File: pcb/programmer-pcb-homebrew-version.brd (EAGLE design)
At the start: 17 x 56.9 mm, 10 parts, among them IC1 MEGA8-AI, IC2 FT232RL, Q1 16 MHz

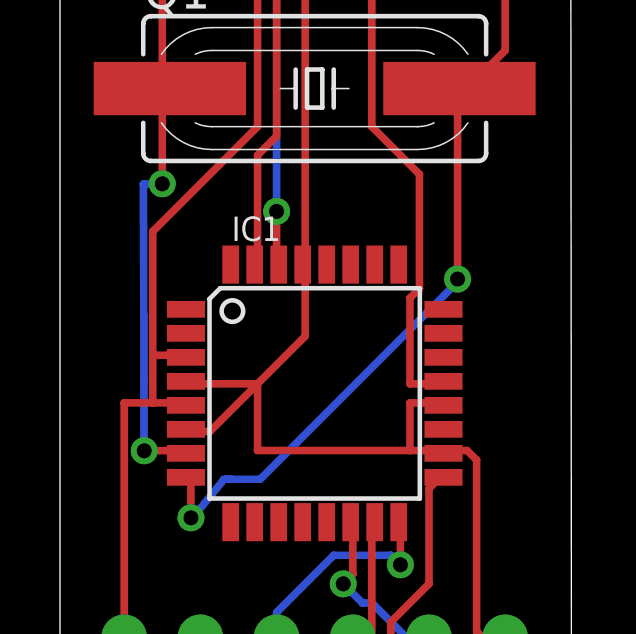
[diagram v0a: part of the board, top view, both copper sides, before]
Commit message: Revert "Minor changes"
This reverts commit 5d468dcfe678118c8d189d65b8291410209d50cf.
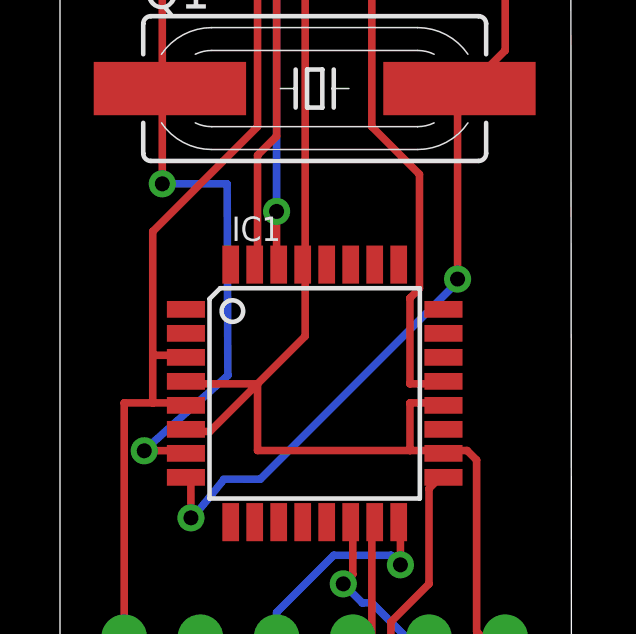
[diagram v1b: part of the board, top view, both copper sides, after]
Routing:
- net N$4: track 10.7 -> 12.2 mm
- net S$28: track 8.90 -> 10.2 mm
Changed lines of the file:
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@@
 <contactref element="C2" pad="1"/>
 <contactref element="Q1" pad="1"/>
-<wire x1="5.08" y1="19.685" x2="4.44785625" y2="19.67254375" width="0.254" layer="16"/>
+<wire x1="5.08" y1="19.685" x2="7.240178125" y2="19.685" width="0.254" layer="16"/>
 <wire x1="5.08" y1="22.86" x2="5.08" y2="19.685" width="0.254" layer="1"/>
 <wire x1="5.08" y1="22.86" x2="5.08" y2="29.21" width="0.254" layer="1"/>
@@
 </signal>
 <signal name="S$28">
-<wire x1="4.44874375" y1="19.67405" x2="4.47365" y2="13.184984375" width="0.254" layer="16"/>
-<wire x1="4.47365" y1="13.184984375" x2="4.468321875" y2="10.791303125" width="0.254" layer="16"/>
+<wire x1="7.241165625" y1="19.67993125" x2="7.265975" y2="13.297084375" width="0.254" layer="16"/>
+<wire x1="7.265975" y1="13.297084375" x2="4.468321875" y2="10.791303125" width="0.254" layer="16"/>
 <wire x1="4.468321875" y1="10.791303125" x2="4.47433125" y2="10.780275" width="0.254" layer="16"/>
 </signal>

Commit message: Minor changes
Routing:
- net N$4: track 12.2 -> 10.7 mm
- net S$28: track 10.2 -> 8.90 mm
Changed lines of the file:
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@@
 <contactref element="C2" pad="1"/>
 <contactref element="Q1" pad="1"/>
-<wire x1="5.08" y1="19.685" x2="7.240178125" y2="19.685" width="0.254" layer="16"/>
+<wire x1="5.08" y1="19.685" x2="4.44785625" y2="19.67254375" width="0.254" layer="16"/>
 <wire x1="5.08" y1="22.86" x2="5.08" y2="19.685" width="0.254" layer="1"/>
 <wire x1="5.08" y1="22.86" x2="5.08" y2="29.21" width="0.254" layer="1"/>
@@
 </signal>
 <signal name="S$28">
-<wire x1="7.241165625" y1="19.67993125" x2="7.265975" y2="13.297084375" width="0.254" layer="16"/>
-<wire x1="7.265975" y1="13.297084375" x2="4.468321875" y2="10.791303125" width="0.254" layer="16"/>
+<wire x1="4.44874375" y1="19.67405" x2="4.47365" y2="13.184984375" width="0.254" layer="16"/>
+<wire x1="4.47365" y1="13.184984375" x2="4.468321875" y2="10.791303125" width="0.254" layer="16"/>
 <wire x1="4.468321875" y1="10.791303125" x2="4.47433125" y2="10.780275" width="0.254" layer="16"/>
 </signal>
